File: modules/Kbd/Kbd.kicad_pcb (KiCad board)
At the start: 2 copper layers, 40.6 x 40.6 mm, 43 parts, among them J1 2, J10 11, J11 12, J12 13, J13 A0, J14 A1, J15 A2, J16 A3, J17 A4, J18 A5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

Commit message: Kbd. Lost tracks.
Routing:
- net Net-(D10-Pad2): track 5.27 -> 45.0 mm
- net Net-(D12-Pad1): track 38.9 -> 64.9 mm
- net Net-(D11-Pad1): track 30.7 -> 56.7 mm
- net Net-(D1-Pad1): track 20.5 -> 46.5 mm
- net Net-(D1-Pad2): track 29.3 -> 48.8 mm
- net Net-(D7-Pad2): track 23.7 -> 43.2 mm
- net Net-(D4-Pad2): track 23.1 -> 42.6 mm
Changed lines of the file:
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@@
-(kicad_pcb (version 20171130) (host pcbnew "(5.1.4)-1")
+(kicad_pcb (version 20171130) (host pcbnew "(5.1.5)-3")
   (general
     (thickness 1.6)
     (drawings 30)
-    (tracks 90)
+    (tracks 119)
     (zones 0)
     (modules 43)
@@
   (segment (start 96.86 62.715) (end 95.885 61.74) (width 0.8) (layer B.Cu) (net 18))
   (segment (start 98.7425 62.715) (end 96.86 62.715) (width 0.8) (layer B.Cu) (net 18))
+  (segment (start 98.7425 52.555) (end 98.7425 59.055) (width 0.8) (layer F.Cu) (net 18))
+  (segment (start 98.7425 62.715) (end 98.7425 69.215) (width 0.8) (layer F.Cu) (net 18))
+  (segment (start 98.7425 72.875) (end 98.7425 79.375) (width 0.8) (layer F.Cu) (net 18))
+  (segment (start 98.7425 83.035) (end 98.7425 89.535) (width 0.8) (layer F.Cu) (net 18))
   (segment (start 103.2425 52.555) (end 103.2425 53.969213) (width 0.8) (layer B.Cu) (net 19))
   (segment (start 103.2425 53.969213) (end 103.883287 54.61) (width 0.8) (layer B.Cu) (net 19))
@@
   (segment (start 122.555 57.785) (end 122.555 59.845) (width 0.8) (layer B.Cu) (net 19))
   (segment (start 119.7525 52.555) (end 119.7525 54.61) (width 0.8) (layer B.Cu) (net 19))
+  (segment (start 103.2425 52.555) (end 103.2425 59.055) (width 0.8) (layer F.Cu) (net 19))
+  (segment (start 111.4975 52.555) (end 111.4975 59.055) (width 0.8) (layer F.Cu) (net 19))
+  (segment (start 119.7525 52.555) (end 119.7525 59.055) (width 0.8) (layer F.Cu) (net 19))
   (segment (start 106.9975 59.055) (end 106.9975 62.715) (width 0.8) (layer B.Cu) (net 20))
   (segment (start 106.9975 69.215) (end 106.9975 72.875) (width 0.8) (layer B.Cu) (net 20))
@@
   (segment (start 107.4875 58.565) (end 106.9975 59.055) (width 0.8) (layer B.Cu) (net 20))
   (segment (start 109.22 58.565) (end 107.4875 58.565) (width 0.8) (layer B.Cu) (net 20))
+  (segment (start 106.9975 52.555) (end 106.9975 59.055) (width 0.8) (layer F.Cu) (net 20))
+  (segment (start 106.9975 62.715) (end 106.9975 69.215) (width 0.8) (layer F.Cu) (net 20))
+  (segment (start 106.9975 72.875) (end 106.9975 79.375) (width 0.8) (layer F.Cu) (net 20))
+  (segment (start 106.9975 83.035) (end 106.9975 89.535) (width 0.8) (layer F.Cu) (net 20))
   (segment (start 115.2525 59.055) (end 115.2525 62.715) (width 0.8) (layer B.Cu) (net 21))
   (segment (start 115.2525 69.215) (end 115.2525 72.875) (width 0.8) (layer B.Cu) (net 21))
@@
   (segment (start 115.325 58.9825) (end 115.2525 59.055) (width 0.8) (layer B.Cu) (net 21))
   (segment (start 115.325 56.515) (end 115.325 58.9825) (width 0.8) (layer B.Cu) (net 21))
+  (segment (start 115.2525 52.555) (end 115.2525 59.055) (width 0.8) (layer F.Cu) (net 21))
+  (segment (start 115.2525 62.715) (end 115.2525 69.215) (width 0.8) (layer F.Cu) (net 21))
+  (segment (start 115.2525 72.875) (end 115.2525 79.375) (width 0.8) (layer F.Cu) (net 21))
+  (segment (start 115.2525 83.035) (end 115.2525 89.535) (width 0.8) (layer F.Cu) (net 21))
   (segment (start 103.2425 64.129213) (end 103.883287 64.77) (width 0.8) (layer B.Cu) (net 22))
   (segment (start 103.2425 62.715) (end 103.2425 64.129213) (width 0.8) (layer B.Cu) (net 22))
@@
   (segment (start 117.602 66.012) (end 117.63 66.04) (width 0.8) (layer B.Cu) (net 22))
   (segment (start 117.602 64.77) (end 117.602 66.012) (width 0.8) (layer B.Cu) (net 22))
+  (segment (start 119.7525 62.715) (end 119.7525 69.215) (width 0.8) (layer F.Cu) (net 22))
+  (segment (start 111.4975 62.715) (end 111.4975 69.215) (width 0.8) (layer F.Cu) (net 22))
+  (segment (start 103.2425 62.715) (end 103.2425 69.215) (width 0.8) (layer F.Cu) (net 22))
   (segment (start 103.2425 74.289213) (end 103.883287 74.93) (width 0.8) (layer B.Cu) (net 23))
   (segment (start 103.2425 72.875) (end 103.2425 74.289213) (width 0.8) (layer B.Cu) (net 23))
@@
   (segment (start 117.63 74.958) (end 117.63 76.708) (width 0.8) (layer B.Cu) (net 23))
   (segment (start 117.602 74.93) (end 117.63 74.958) (width 0.8) (layer B.Cu) (net 23))
+  (segment (start 103.2425 72.875) (end 103.2425 79.375) (width 0.8) (layer F.Cu) (net 23))
+  (segment (start 111.4975 72.875) (end 111.4975 79.375) (width 0.8) (layer F.Cu) (net 23))
+  (segment (start 119.7525 72.875) (end 119.7525 79.375) (width 0.8) (layer F.Cu) (net 23))
   (segment (start 119.7525 83.035) (end 118.133 83.035) (width 0.8) (layer B.Cu) (net 24))
   (segment (start 117.348 83.82) (end 117.348 86.36) (width 0.8) (layer B.Cu) (net 24))
   (segment (start 118.133 83.035) (end 117.348 83.82) (width 0.8) (layer B.Cu) (net 24))
+  (segment (start 103.2425 85.4625) (end 103.2425 83.035) (width 0.8) (layer B.Cu) (net 24))
+  (segment (start 104.14 86.36) (end 103.2425 85.4625) (width 0.8) (layer B.Cu) (net 24))
+  (segment (start 111.4975 83.035) (end 111.4975 86.36) (width 0.8) (layer B.Cu) (net 24))
+  (segment (start 117.348 86.36) (end 111.4425 86.36) (width 0.8) (layer B.Cu) (net 24))
+  (segment (start 111.4425 86.36) (end 104.14 86.36) (width 0.8) (layer B.Cu) (net 24))
+  (segment (start 103.2425 83.035) (end 103.2425 89.535) (width 0.8) (layer F.Cu) (net 24))
+  (segment (start 111.4975 83.035) (end 111.4975 89.535) (width 0.8) (layer F.Cu) (net 24))
+  (segment (start 119.7525 83.035) (end 119.7525 89.535) (width 0.8) (layer F.Cu) (net 24))
 )

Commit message: Kbd v2. Fixed pin numbering.
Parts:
- moved VD1 25.6 mm to (119.1, 36.2), turned to 180 degrees
- moved R3 20.4 mm to (112.5, 36.2)
- moved J16 20.3 mm to (92.7, 54.6)
- moved J18 20.3 mm to (92.7, 59.7)
- moved J2 20.3 mm to (125.7, 59.7)
- moved J4 20.3 mm to (125.7, 54.6)
- moved D1 20.3 mm to (98.7, 38.7)
- moved D2 20.3 mm to (107.0, 38.7)
- moved D3 20.3 mm to (115.3, 38.7)
- moved D4 20.3 mm to (98.7, 48.9)
- moved D5 20.3 mm to (107.0, 48.9)
- moved D6 20.3 mm to (115.3, 48.9)
- moved D7 20.3 mm to (98.7, 59.1)
- moved D8 20.3 mm to (107.0, 59.1)
- moved D9 20.3 mm to (115.3, 59.1)
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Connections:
- VD1 pad 1: Net-(J6-Pad1) -> Net-(J10-Pad1)
- VD2 pad 1: Net-(J5-Pad1) -> Net-(J9-Pad1)
- VD3 pad 1: Net-(J4-Pad1) -> Net-(J8-Pad1)
- VD4 pad 1: Net-(J3-Pad1) -> Net-(J7-Pad1)
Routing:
- net Net-(J7-Pad1): track 0.00 -> 21.8 mm
- net Net-(J8-Pad1): track 0.00 -> 14.8 mm
- net Net-(J3-Pad1): track 11.9 -> 0.00 mm
- net Net-(J5-Pad1): track 9.45 -> 0.00 mm
- net Net-(J9-Pad1): track 0.00 -> 8.78 mm
- net Net-(J6-Pad1): track 8.68 -> 0.00 mm
- net Net-(J10-Pad1): track 0.00 -> 7.18 mm
- net Net-(D1-Pad2): track 48.8 -> 42.4 mm
- net Net-(J4-Pad1): track 5.47 -> 0.00 mm
- net Net-(J19-Pad1): track 23.0 -> 21.2 mm
- net Net-(D12-Pad1): track 64.9 -> 66.2 mm
- net Net-(D4-Pad2): track 42.6 -> 42.0 mm
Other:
- board text added: "26.04.2020"
- board text added: "D0"
- board text added: "D1"
- board text added: "D2"
- board text added: "D3"
- board text added: "Line0"
- board text added: "Line1"
- board text added: "Line2"
- board text added: "hash"
- board text added: "v2"

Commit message: Kbd. Add photomask in pdf.
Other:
- board text added: "edac1a"
- board text removed: "hash"
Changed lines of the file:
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@@
     )
   )
-  (gr_text hash (at 95.885 60.96 90) (layer B.Cu)
+  (gr_text edac1a (at 95.885 60.96 90) (layer B.Cu)
     (effects (font (size 1 1) (thickness 0.2)) (justify mirror))
   )

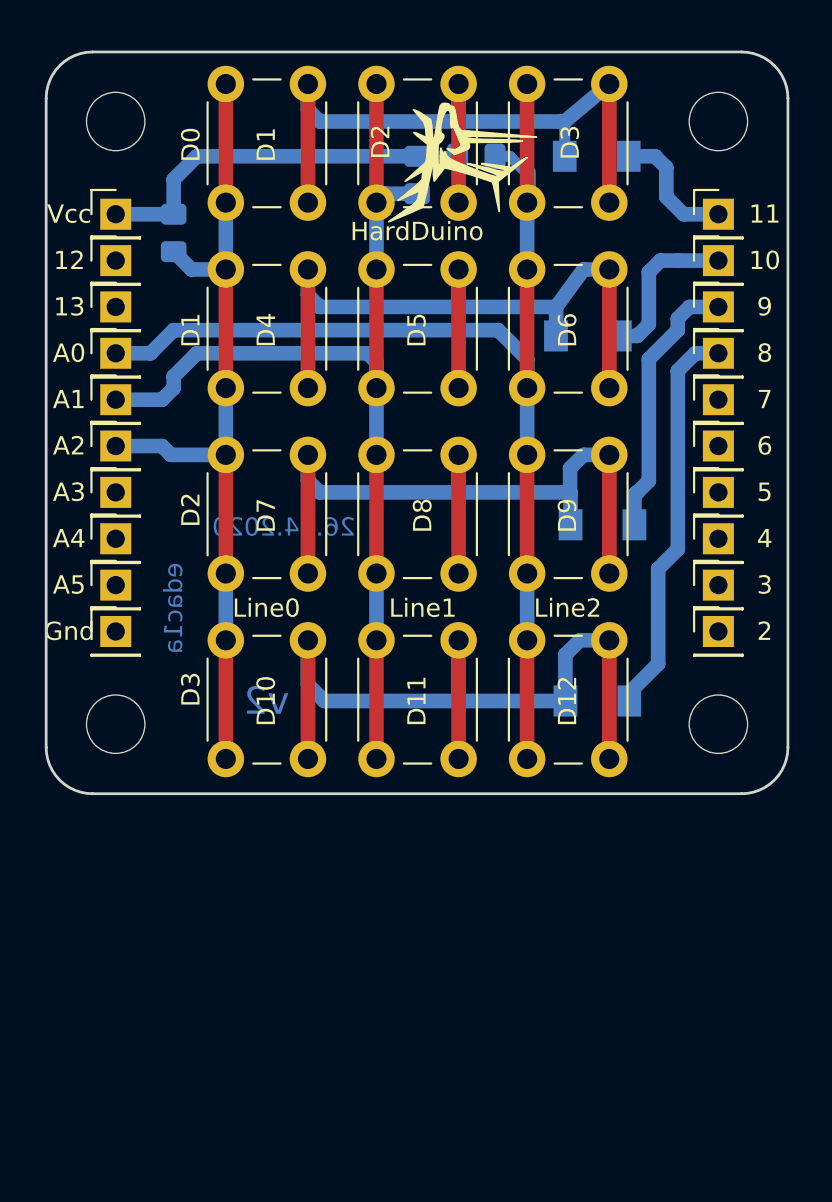
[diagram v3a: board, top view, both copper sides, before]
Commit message: 1x PCBs. Move holes to edges. Caution! This changes is uncompatible with previous versions...
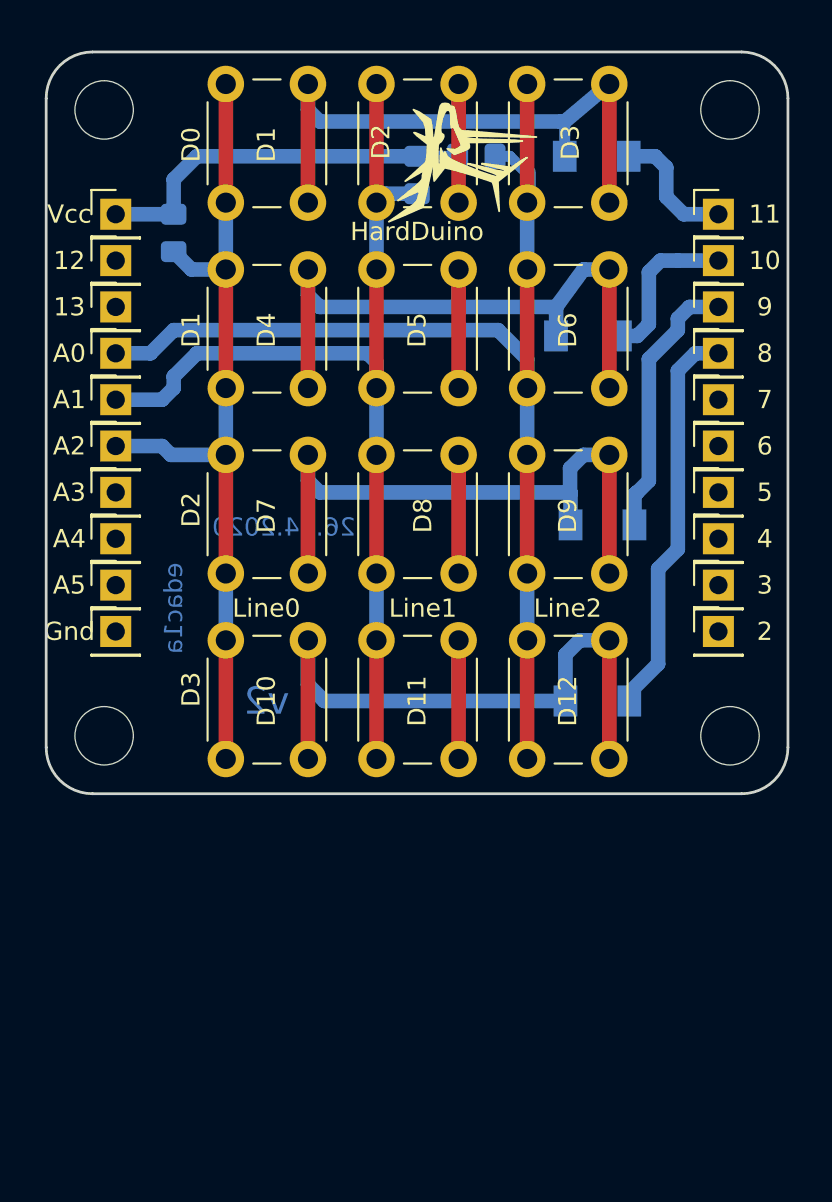
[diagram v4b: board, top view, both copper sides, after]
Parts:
- moved H1 0.90 mm to (92.1, 33.7)
- moved H3 0.90 mm to (126.4, 33.7)
- moved H2 0.90 mm to (92.1, 67.9)
- moved H4 0.90 mm to (126.4, 67.9)
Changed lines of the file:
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@@
   )
   (module MountingHole:MountingHole_3.2mm_M3 (layer F.Cu)
-    (at 92.71 34.29)
+    (at 92.0750 33.6550)
     (descr "Mounting Hole 3.2mm, no annular, M3")
     (tags "mounting hole 3.2mm no annular m3")
@@
   )
   (module MountingHole:MountingHole_3.2mm_M3 (layer F.Cu)
-    (at 92.71 67.31)
+    (at 92.0750 67.9450)
     (descr "Mounting Hole 3.2mm, no annular, M3")
     (tags "mounting hole 3.2mm no annular m3")
@@
   )
   (module MountingHole:MountingHole_3.2mm_M3 (layer F.Cu)
-    (at 125.73 34.29)
+    (at 126.3650 33.6550)
     (descr "Mounting Hole 3.2mm, no annular, M3")
     (tags "mounting hole 3.2mm no annular m3")
@@
   )
   (module MountingHole:MountingHole_3.2mm_M3 (layer F.Cu)
-    (at 125.73 67.31)
+    (at 126.3650 67.9450)
     (descr "Mounting Hole 3.2mm, no annular, M3")
     (tags "mounting hole 3.2mm no annular m3")

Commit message: Fix hash & version
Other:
- board text added: "21.02.2021"
- board text added: "b4d799"
- board text added: "v2.3"
- board text removed: "26.04.2020"
- board text removed: "edac1a"
- board text removed: "v2"

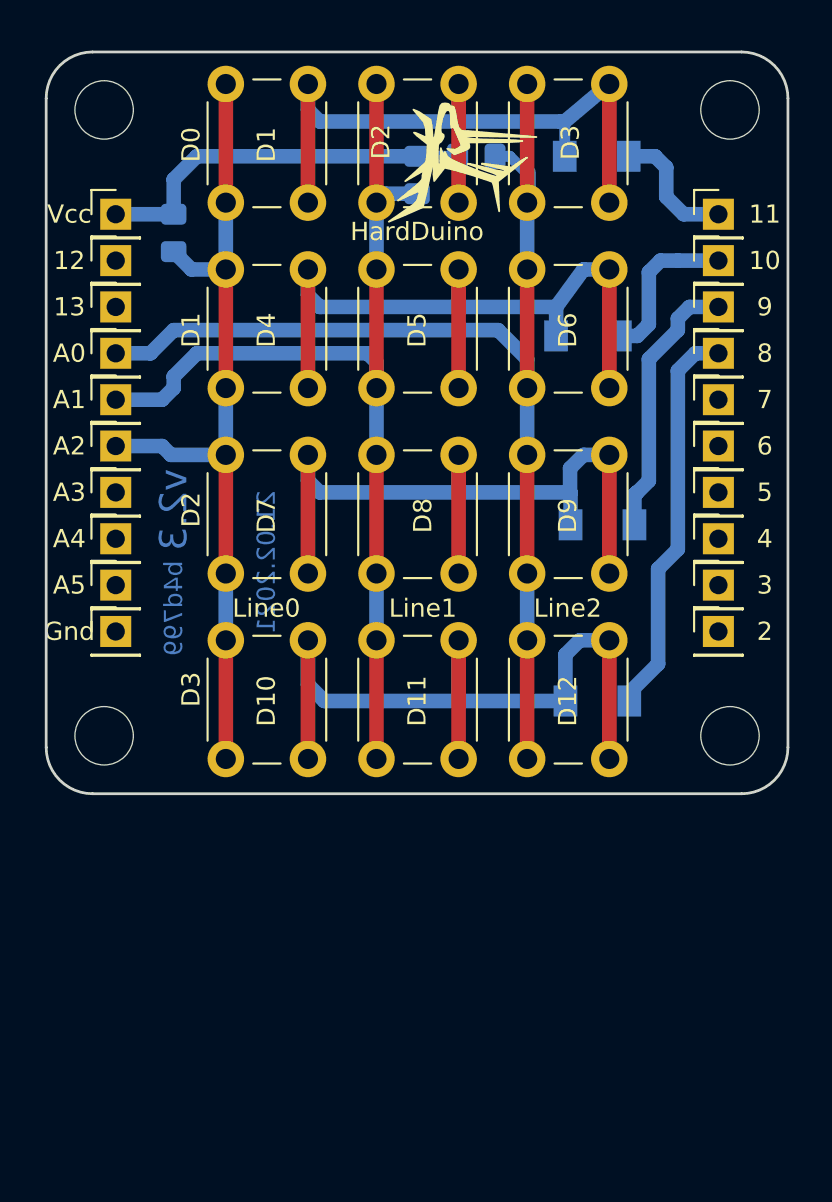
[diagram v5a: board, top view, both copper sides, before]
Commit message: All 1x shields was rotated clockwise
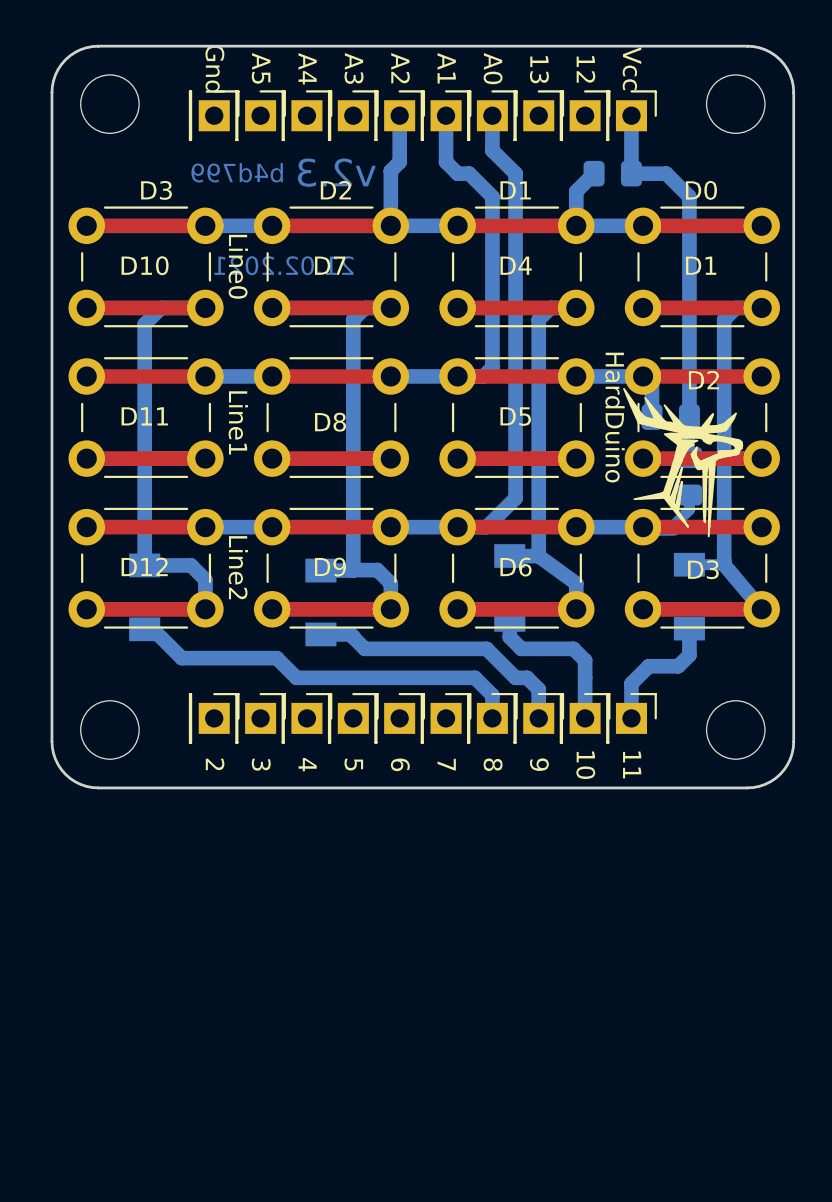
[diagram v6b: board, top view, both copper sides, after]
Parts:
- moved H1 34.6 mm to (126.7, 33.3), turned to 270 degrees
- moved H2 34.6 mm to (92.4, 33.3), turned to 270 degrees
- moved H3 34.0 mm to (126.7, 67.6), turned to 270 degrees
- moved H4 34.0 mm to (92.4, 67.6), turned to 270 degrees
- moved D10 30.2 mm to (91.1, 40.0), turned to 0 degrees
- moved J19 28.8 mm to (121.0, 34.0), turned to 270 degrees
- moved J20 28.8 mm to (98.1, 34.0), turned to 270 degrees
- moved J10 28.0 mm to (121.0, 67.0), turned to 270 degrees
- moved J1 28.0 mm to (98.1, 67.0), turned to 270 degrees
- moved D12 27.3 mm to (91.1, 56.5), turned to 0 degrees
- moved J11 26.9 mm to (118.4, 34.0), turned to 270 degrees
- moved J18 26.9 mm to (100.6, 34.0), turned to 270 degrees
- moved D11 26.3 mm to (91.1, 48.3), turned to 0 degrees
- moved J2 26.1 mm to (100.6, 67.0), turned to 270 degrees
- moved J9 26.1 mm to (118.4, 67.0), turned to 270 degrees
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
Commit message: Now all mounting holes have distance 31.92 x 31.1
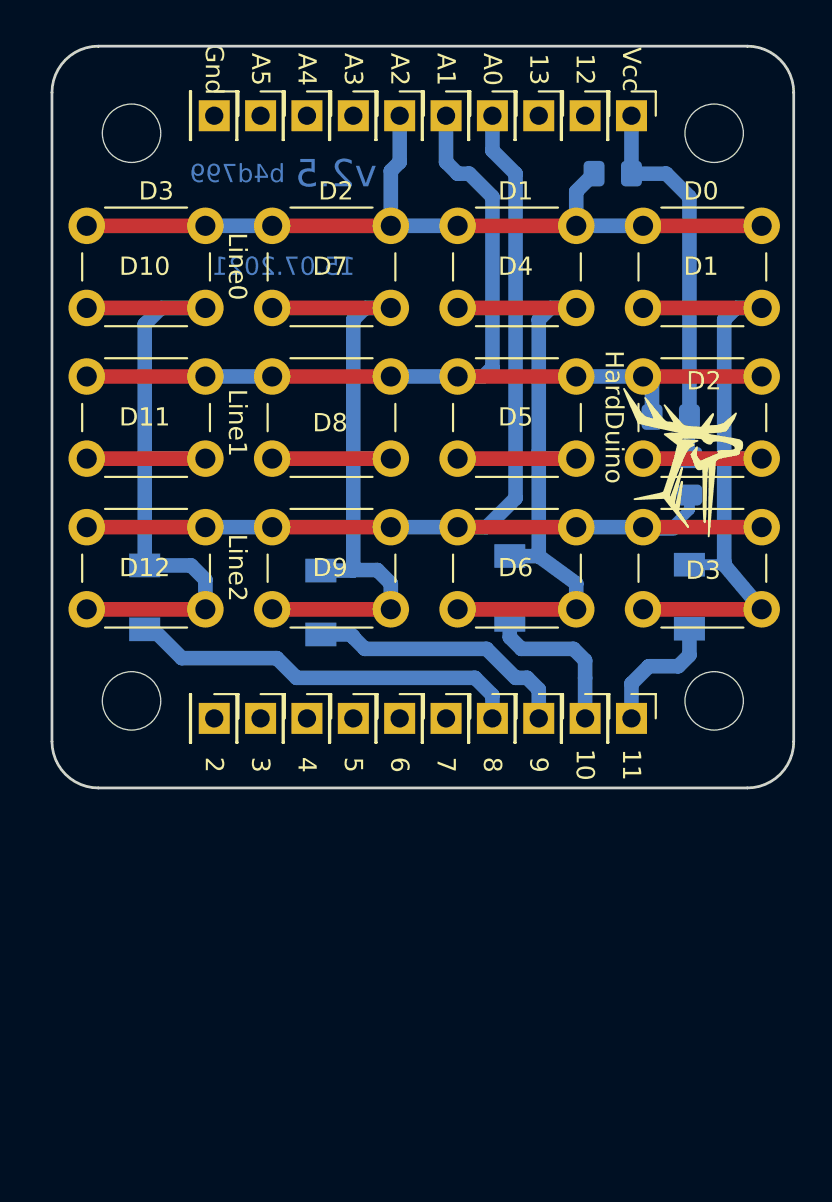
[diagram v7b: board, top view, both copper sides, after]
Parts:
- moved H1 1.99 mm to (125.5, 34.9), turned to 0 degrees
- moved H2 1.99 mm to (93.6, 34.9), turned to 0 degrees
- moved H3 1.99 mm to (125.5, 66.0), turned to 0 degrees
- moved H4 1.99 mm to (93.6, 66.0), turned to 0 degrees
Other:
- board text added: "15.07.2021"
- board text added: "v2.5"
- board text removed: "21.02.2021"
- board text removed: "v2.3"
